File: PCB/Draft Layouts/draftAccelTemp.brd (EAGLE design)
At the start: 4 parts, among them U1 MMA8452Q

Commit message: Aileen's updates
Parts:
- removed ACCEL: 22-23-2041, con-molex:22-23-2041
- removed U1: MMA8452Q, SparkFun-Sensors:QFN-16
- added ACCEL1, ACCEL2, ACCEL3: 22-27-2041-04, con-molex:6410-04
- added C1: 1uF, rcl:C0805
- added D1, D2, D3, D4: 1N4004, diode:DO41-10
- added ECG: 22-27-2021-02, con-molex:6410-02
- added FRAM: 22-27-2081-08, con-molex:6410-08
- added IC3: AD623R, analog-devices:SO8
- added R1, R2, R3: (no value), rcl:R0805
- added R4, R5: 330k, rcl:R0805
- added R6, R7: 560k, rcl:R0805
- TEMP: value 22-23-2041 -> 22-27-2081-08; device con-molex:22-23-2041 -> con-molex:6410-08
- moved TEMP 7.41 mm to (-29.2, -76.2)
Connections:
- removed net N$3: TEMP.3
- new net A0: ACCEL3.4, TEMP.5
- new net A0FRAM: FRAM.1
- new net A1: TEMP.6
- new net A1FRAM: FRAM.2
- new net A2: TEMP.7
- new net A2FRAM: FRAM.3
- new net AGND: FRAM.4, FRAM.6, IC3.5
- new net N$5: D1.A, D2.C, IC3.3, R4.2
- new net N$6: C1.1, IC3.6
- new net N$7: IC3.8, R6.2
- new net N$8: IC3.1, R6.1
- new net OS: R3.2, TEMP.4
- net GND: now also ACCEL1.4, ACCEL2.4, C1.2, D1.C, D2.A, D3.A, D4.C, IC3.4, R7.1, R7.2, TEMP.8; no longer ACCEL.4, U1.10, U1.12, U1.5
- net N$1: now also ECG.1, R4.1; no longer TEMP.1
- net N$2: now also D3.C, D4.A, IC3.2, R5.1; no longer TEMP.2
- net N$4: now also ECG.2, R5.2; no longer TEMP.4
- net SCL: now also ACCEL1.3, ACCEL2.3, FRAM.7, R2.2, TEMP.3; no longer ACCEL.3, U1.4
- net SDA: now also ACCEL1.2, ACCEL2.2, FRAM.8, R1.2, TEMP.2; no longer ACCEL.2, U1.6
- net VCC: now also ACCEL1.1, ACCEL2.1, FRAM.5, IC3.7, R1.1, R2.1, R3.1, TEMP.1; no longer ACCEL.1, U1.1, U1.14

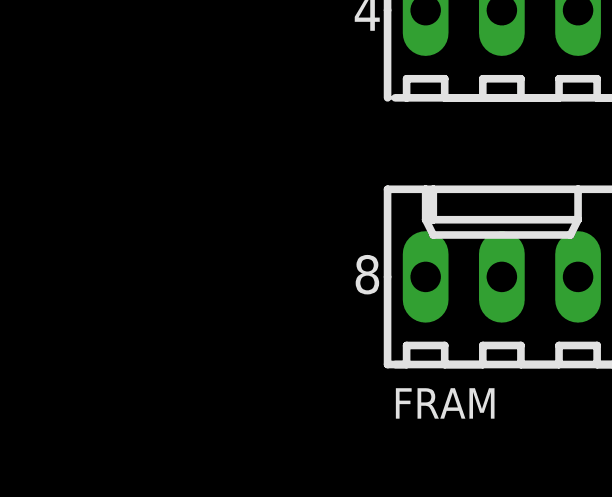
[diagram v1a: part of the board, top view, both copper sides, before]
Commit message: new custom parts library
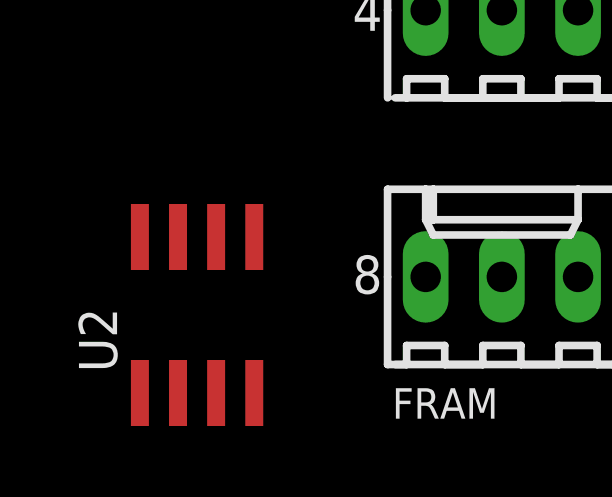
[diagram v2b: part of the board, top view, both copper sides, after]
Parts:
- added U2: MB85RC256VPF-G-JNERE2, Custom Parts:SOIC8
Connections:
- new net N$10: U2.7
- new net N$3: U2.6
- new net N$9: U2.5
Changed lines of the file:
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@@
 <?xml version="1.0" encoding="utf-8"?>
 <!DOCTYPE eagle SYSTEM "eagle.dtd">
-<eagle version="9.2.1">
+<eagle version="9.2.2">
 <drawing>
 <settings>
@@
 <layers>
 <layer number="1" name="Top" color="4" fill="1" visible="yes" active="yes"/>
+<layer number="2" name="Route2" color="16" fill="1" visible="no" active="yes"/>
+<layer number="3" name="Route3" color="17" fill="1" visible="no" active="yes"/>
+<layer number="4" name="Route4" color="18" fill="1" visible="no" active="yes"/>
+<layer number="5" name="Route5" color="19" fill="1" visible="no" active="yes"/>
+<layer number="6" name="Route6" color="25" fill="1" visible="no" active="yes"/>
+<layer number="7" name="Route7" color="26" fill="1" visible="no" active="yes"/>
+<layer number="8" name="Route8" color="27" fill="1" visible="no" active="yes"/>
+<layer number="9" name="Route9" color="28" fill="1" visible="no" active="yes"/>
+<layer number="10" name="Route10" color="29" fill="1" visible="no" active="yes"/>
+<layer number="11" name="Route11" color="30" fill="1" visible="no" active="yes"/>
+<layer number="12" name="Route12" color="20" fill="1" visible="no" active="yes"/>
+<layer number="13" name="Route13" color="21" fill="1" visible="no" active="yes"/>
+<layer number="14" name="Route14" color="22" fill="1" visible="no" active="yes"/>
+<layer number="15" name="Route15" color="23" fill="1" visible="no" active="yes"/>
 <layer number="16" name="Bottom" color="1" fill="1" visible="yes" active="yes"/>
 <layer number="17" name="Pads" color="2" fill="1" visible="yes" active="yes"/>
@@
 <attribute name="VALUE" x="-36.0411" y="-229.5159" size="0.8128" layer="27" ratio="10"/>
 </element>
+<element name="U2" library="Custom Parts" package="SOIC8" value="MB85RC256VPF-G-JNERE2" x="-55.88" y="-226.06" smashed="yes">
+<attribute name="NAME" x="-58.547" y="-227.965" size="1.27" layer="25" rot="R90"/>
+<attribute name="VALUE" x="-51.943" y="-227.965" size="1.27" layer="27" rot="R90"/>
+</element>
 </elements>
 <signals>
@@
 <wire x1="-38.1" y1="-224.79" x2="-43.18" y2="-224.79" width="0" layer="19" extent="1-1"/>
 </signal>
+<signal name="N$3">
+<contactref element="U2" pad="6"/>
+</signal>
+<signal name="N$9">
+<contactref element="U2" pad="5"/>
+</signal>
+<signal name="N$10">
+<contactref element="U2" pad="7"/>
+</signal>
 </signals>
